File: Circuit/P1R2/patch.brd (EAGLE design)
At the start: 50.8 x 53.1 mm, 66 parts, among them U1 MK20DX256VLH7, U2 TPS61200, U3 MPU-9250, Y1 32.768KHz, Y2 16Mhz/8pF, Y3 16 Mhz, Y4 16 Mhz

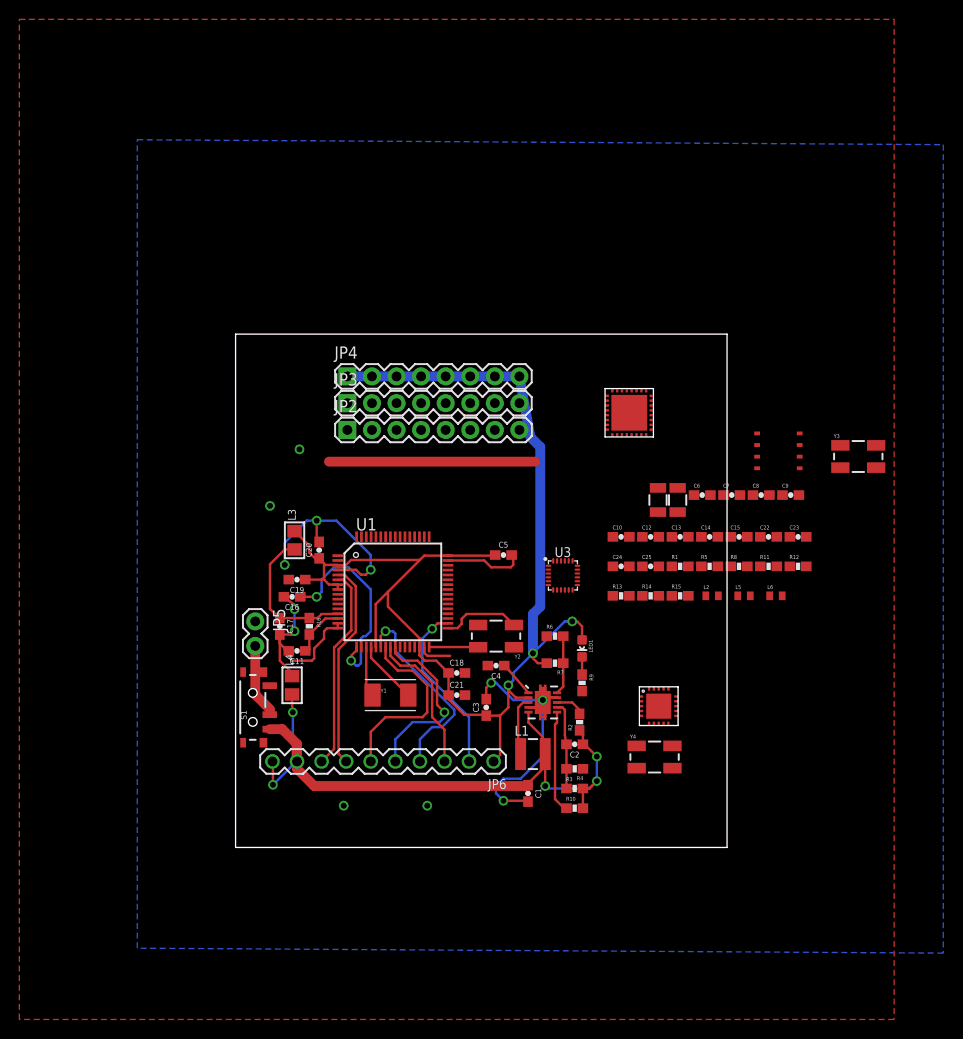
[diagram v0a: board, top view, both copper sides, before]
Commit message: Mesh and IMU in place
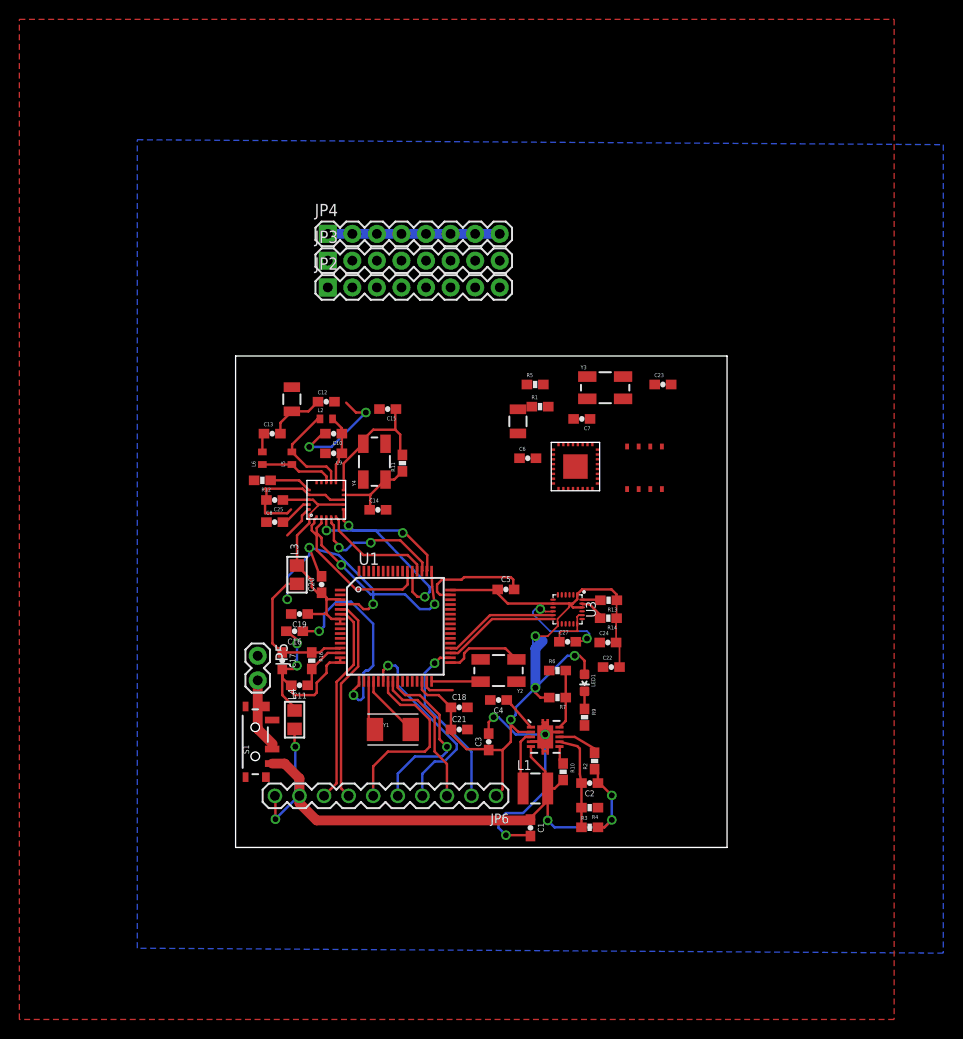
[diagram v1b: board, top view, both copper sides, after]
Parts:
- removed MESH: NRF24L01, RF:QFN20(4X4)
- removed R15: 10k, SparkFun-Resistors:0603-RES
- removed R8: 12k, SparkFun-Resistors:0603-RES
- removed WIFI: ESP8266EX, wifi:QFN32
- added C27: .1 uF, SparkFun-Capacitors:0603-CAP
- added U$4: NRF24L01, RF:QFN20(4X4)
- added U$6: ESP8266EX, wifi:QFN32
- Y3: value 16 Mhz -> 26 Mhz
- moved R12 56.1 mm to (2.77, 37.9), turned to 180 degrees
- moved L6 55.0 mm to (2.77, 40.2), turned to 90 degrees
- moved C8 50.4 mm to (4.04, 33.6)
- moved L5 48.9 mm to (5.82, 40.2), turned to 90 degrees
- moved C9 47.4 mm to (10.1, 40.7), turned to 180 degrees
- moved L2 43.9 mm to (9.37, 44.3)
- moved C13 43.5 mm to (3.78, 42.8)
- moved Y4 42.1 mm to (14.4, 39.9), turned to 90 degrees
- moved U$2 41.2 mm to (5.82, 46.3), turned to 180 degrees
- moved C25 39.5 mm to (4.04, 35.9), turned to 180 degrees
- moved R11 39.3 mm to (17.2, 39.7), turned to 90 degrees
- moved C15 38.6 mm to (15.7, 45.3), turned to 180 degrees
- moved C12 36.3 mm to (9.37, 46.1)
- moved C14 34.4 mm to (14.7, 34.9)
- moved C10 31.6 mm to (10.1, 42.8), turned to 180 degrees
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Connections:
- net 14 renamed PTD1
- net 2 renamed PTD0
- net 21 renamed PTD6
- net 23 renamed PTC2
- net 24 renamed PTA5
- net 26 renamed PTE1
- net 29 renamed PTC10
- net 3 renamed PTA12
- net 30 renamed PTC11
- net 31 renamed PTE0
- net 33 renamed PTA4
- net 4 renamed PTA13
- net 5 renamed PTD7
- net 6 renamed PTD4
- net 7 renamed PTD2
- net 8 renamed PTD3
- net 9 renamed PTC3
- net N$7 renamed PTD5
- removed net 0: U1.39
- removed net 1: U1.40
- removed net 10: U1.49
- removed net 11/MOSI: U1.51
- removed net 12/MISO: U1.52
- removed net 13/SCK: U1.50
- removed net 15: U1.43
- removed net 22: U1.44
- removed net 25: U1.42
- removed net 27: U1.54
- removed net 3.3V1: C22.2, C24.2, C25.1, MESH.15, MESH.18, MESH.7, R8.2, U$3.8, U3.1, U3.13, U3.8, WIFI.CHIP_EN/7, WIFI.VDD3P3/3, WIFI.VDD3P3/4, WIFI.VDDA/1, WIFI.VDDD/29, WIFI.VDDPST/11, WIFI.VDDPST/17
- removed net 32: U1.41
- removed net CE: MESH.1
- removed net CSN: MESH.2
- removed net GND1: C10.2, C12.2, C14.2, C15.2, C22.1, C23.2, C24.1, C25.2, C7.2, C8.1, C9.2, MESH.14, MESH.17, MESH.20, MESH.8, R12.2, R5.1, U$3.4, WIFI.GND
- removed net IQR: MESH.6
- removed net MISO: MESH.5
- removed net MOSI: MESH.4
- removed net N$22: MESH.GND
- removed net N$31: R8.1, WIFI.GPIO2/14
- removed net N$33: U3.11
- removed net N$35: U3.21
- removed net N$36: U3.7
- removed net N$37: U3.18, U3.20
- removed net N$39: U3.12
- removed net N$40: U3.22
- removed net RST: R1.1, WIFI.EXT_RSTB/32
- removed net RX_W: WIFI.U0TXD/26
- removed net SCK: MESH.3
- removed net SDO: R15.2
- removed net TX_W: WIFI.U0RXD/25
- new net PTB16: U$6.U0RXD/25, U1.39
- new net PTB17: U$6.U0TXD/26, U1.40
- new net PTB18: U$6.GPIO0/15, U1.41
- new net PTB19: U$6.GPIO2/14, U1.42
- new net PTC0: U$6.EXT_RSTB/32, U1.43
- new net PTC1: U$6.CHIP_EN/7, U1.44
- new net PTC4: U$4.2, U1.49
- new net PTC5: U$4.3, U1.50
- new net PTC6: U$4.4, U1.51
- new net PTC7: U$4.5, U1.52
- new net PTC8: U$4.6, U1.53
- new net PTC9: U$4.1, U1.54
- net 3.3V: now also C22.2, C24.2, C25.1, R13.1, R14.1, U$3.8, U$4.18, U$4.7, U$6.VDD3P3/3, U$6.VDD3P3/4, U$6.VDDA/1, U$6.VDDD/29, U$6.VDDPST/11, U$6.VDDPST/17, U3.1, U3.13, U3.22, U3.8
- net GND: now also C10.2, C12.2, C14.2, C15.2, C22.1, C23.2, C24.1, C25.2, C27.1, C7.2, C8.1, C9.2, R1.2, R12.2, R5.1, U$3.4, U$4.17, U$4.20, U$4.8, U$6.GND, U3.18, U3.20
- net N$13: now also U$6.LNA/2; no longer WIFI.LNA/2
- net N$17: now also U$4.9; no longer MESH.9
- net N$18: now also U$4.10; no longer MESH.10
- net N$19: now also U$4.11; no longer MESH.11
- net N$20: now also U$4.13; no longer MESH.13
- net N$21: now also U$4.19; no longer MESH.19
- net N$23: now also U$4.12; no longer MESH.12
- net N$24: now also U$4.16; no longer MESH.16
- net N$32: now also U$6.MTCK/12; no longer WIFI.MTCK/12
- net N$34: now also C27.2
- net N$38: now also R1.1, U$6.RES12K/31; no longer WIFI.RES12K/31
- net PTB0: now also U3.12
- net PTB1: now also U3.11
- net RTC: now also U$6.VDD_RTC/5; no longer WIFI.VDD_RTC/5
- net SCL: now also U3.23
- net SD-CLK: now also U$6.SD_CLK/21; no longer WIFI.SD_CLK/21
- net SD-CMD: now also U$6.SD_CMD/20; no longer WIFI.SD_CMD/20
- net SD-D0: now also U$6.SD_DATA_0/22; no longer WIFI.SD_DATA_0/22
- net SD-D1: now also U$6.SD_DATA_1/23; no longer WIFI.SD_DATA_1/23
- net SD-D2: now also U$6.SD_DATA_2/18; no longer WIFI.SD_DATA_2/18
- net SD-D3: now also U$6.SD_DATA_3/19; no longer WIFI.SD_DATA_3/19
- net SDA: now also U3.24
- net TOUT: now also U$6.TOUT/6; no longer WIFI.TOUT/6
- net VDD: now also U$6.VDDA/30; no longer R13.1, R14.1, R15.1, WIFI.VDDA/30
- net XTAL_IN: now also U$6.XTAL_IN/28; no longer WIFI.XTAL_IN/28
- net XTAL_OUT: now also U$6.XTAL_OUT/27; no longer WIFI.XTAL_OUT/27
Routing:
- net PTC4: track 0.00 -> 21.4 mm, vias 0 -> 2
- net GND: track 102.5 -> 121.1 mm, vias 8 -> 10
- net PTC8: track 0.00 -> 17.8 mm, vias 0 -> 2
- net PTC9: track 0.00 -> 16.5 mm
- net N$18: track 0.00 -> 14.9 mm
- net PTC5: track 0.00 -> 14.5 mm, vias 0 -> 2
- net PTC6: track 0.00 -> 14.5 mm, vias 0 -> 2
- net PTB0: track 0.00 -> 12.1 mm
- net PTB1: track 0.00 -> 12.0 mm
- net PTC7: track 0.00 -> 11.7 mm
- net N$34: track 0.00 -> 11.1 mm, vias 0 -> 2
- net N$23: track 0.00 -> 10.8 mm
- net 3.3V: track 132.9 -> 122.9 mm, vias 4 -> 5
- net SOFTPOWER: track 10.7 -> 1.93 mm
- net N$17: track 0.00 -> 8.65 mm
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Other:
- board size 50.8 x 53.1 mm -> 50.8 x 50.8 mm

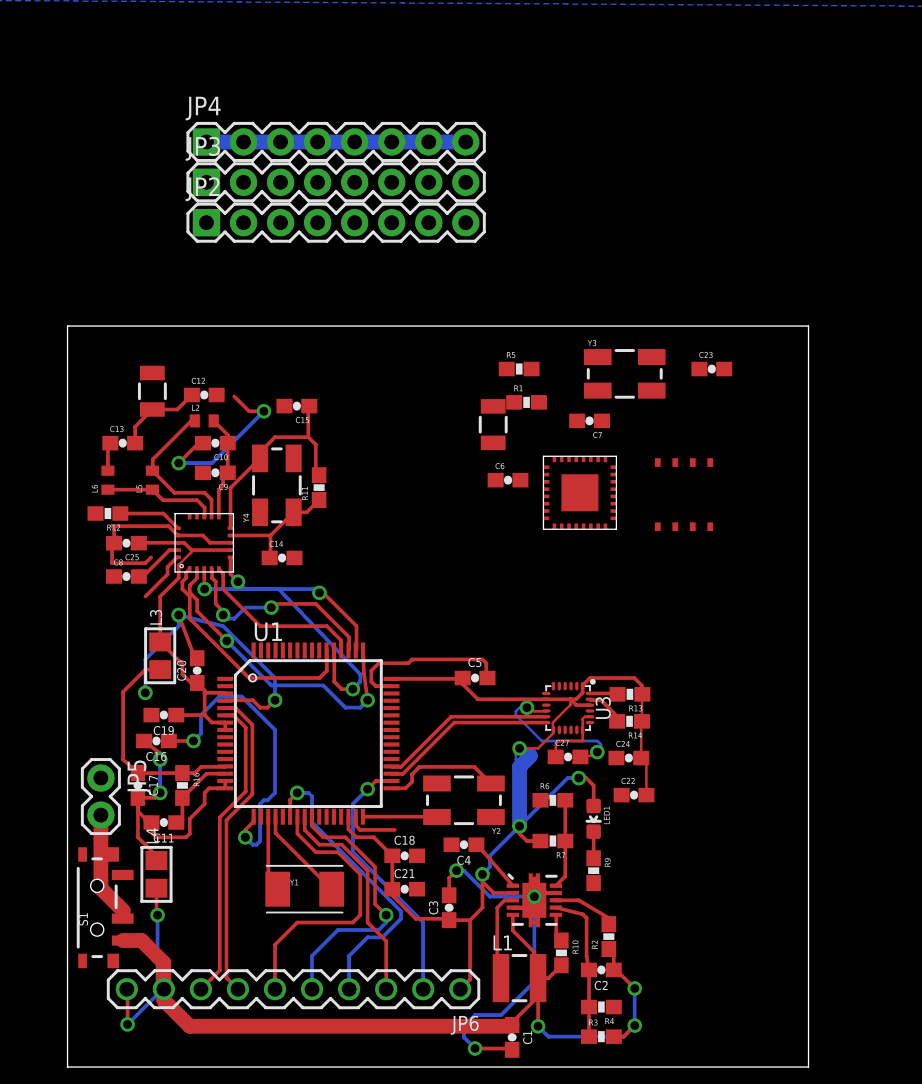
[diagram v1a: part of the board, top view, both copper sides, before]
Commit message: Communications and IMU done. Finishing up GPIO next
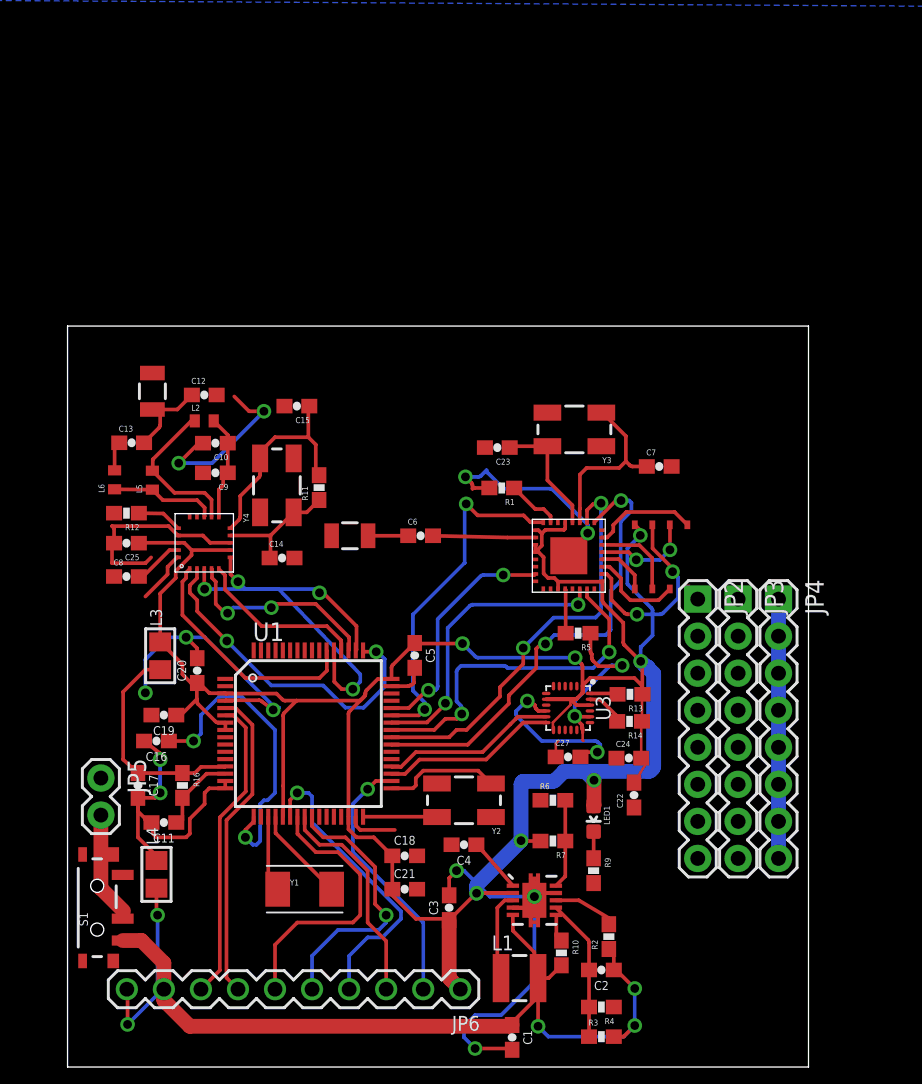
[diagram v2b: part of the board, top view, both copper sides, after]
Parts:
- moved JP4 50.2 mm to (48.7, 32.1), turned to 270 degrees
- moved JP3 46.3 mm to (46.0, 32.1), turned to 270 degrees
- moved JP2 42.4 mm to (43.2, 32.1), turned to 270 degrees
- moved R5 18.6 mm to (35.0, 29.7), turned to 180 degrees
- moved C23 15.7 mm to (29.5, 42.5), turned to 180 degrees
- moved U$1 12.4 mm to (19.4, 36.4), turned to 270 degrees
- moved C6 7.10 mm to (24.2, 36.4)
- moved R1 6.11 mm to (29.8, 39.7), turned to 180 degrees
- moved C7 5.71 mm to (40.6, 41.2), turned to 0 degrees
- moved Y3 5.14 mm to (34.7, 43.7), turned to 180 degrees
- moved U$3 4.55 mm to (40.7, 35.0)
- moved C5 4.42 mm to (23.8, 28.2), turned to 270 degrees
- moved U$6 4.38 mm to (34.4, 35.1)
- moved R12 1.27 mm to (4.04, 38.0)
- moved C13 0.61 mm to (4.39, 42.8)
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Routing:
- net 3.3V: track 122.9 -> 197.3 mm, vias 5 -> 8
- net PTB16: track 0.00 -> 31.9 mm, vias 0 -> 2
- net PTB17: track 0.00 -> 28.4 mm, vias 0 -> 2
- net PTB18: track 0.00 -> 24.4 mm, vias 0 -> 2
- net PTC0: track 0.00 -> 24.2 mm, vias 0 -> 2
- net PTB19: track 0.00 -> 20.2 mm, vias 0 -> 2
- net PTC1: track 0.00 -> 16.4 mm, vias 0 -> 2
- net SD-D2: track 0.00 -> 13.4 mm, vias 0 -> 2
- net XTAL_OUT: track 0.00 -> 12.4 mm
- net GND: track 121.1 -> 133.2 mm, vias 10 -> 14
- net XTAL_IN: track 0.00 -> 8.53 mm
- net SD-D1: track 0.00 -> 7.16 mm
- net N$13: track 0.00 -> 7.01 mm
- net SD-CLK: track 0.00 -> 6.86 mm, vias 0 -> 2
- net SD-D3: track 0.00 -> 6.40 mm
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
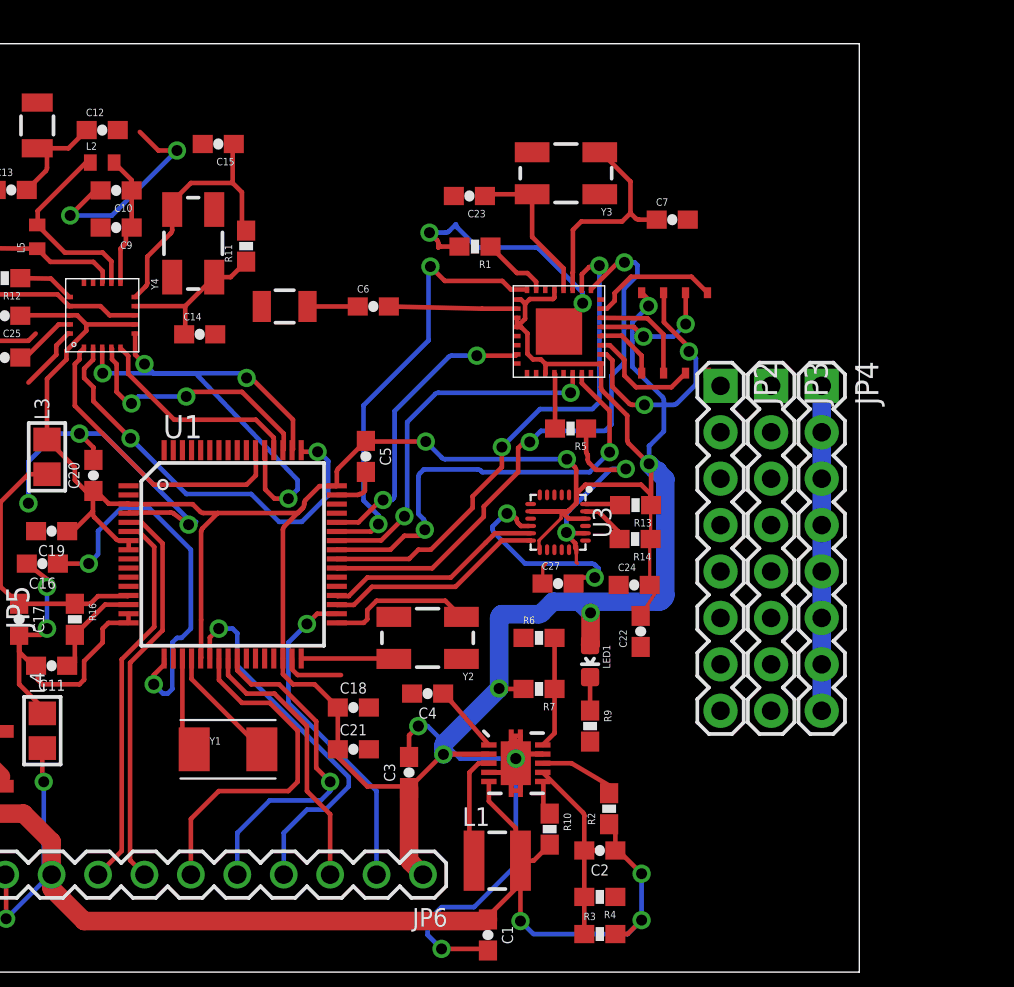
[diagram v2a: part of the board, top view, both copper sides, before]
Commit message: Made space for GPIO. Putting in GPIO and RGB leds
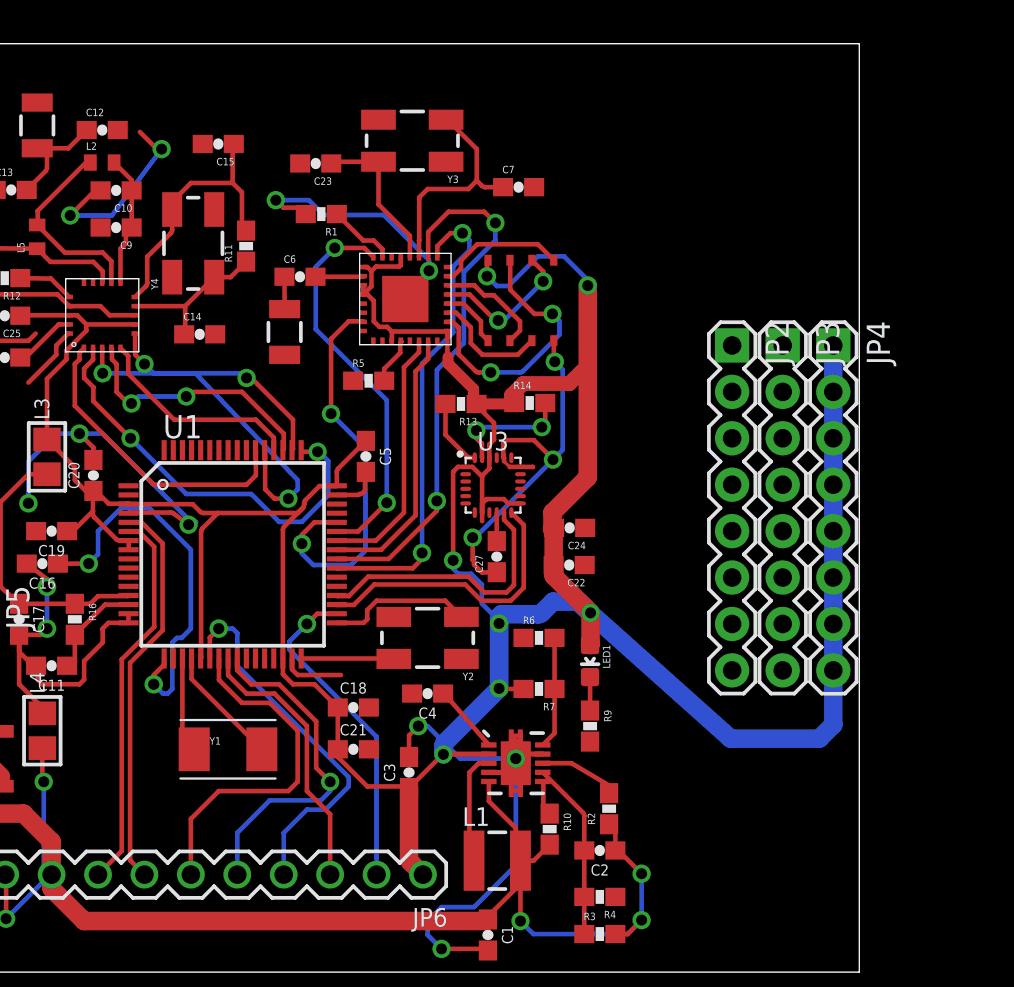
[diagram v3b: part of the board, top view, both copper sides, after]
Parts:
- moved R5 11.4 mm to (24.0, 32.4), turned to 0 degrees
- moved R13 11.0 mm to (29.0, 31.1)
- moved R14 9.41 mm to (32.8, 31.1), turned to 0 degrees
- moved C7 8.59 mm to (32.2, 43.0)
- moved U$3 8.59 mm to (32.3, 36.8)
- moved C23 8.59 mm to (21.1, 44.2)
- moved R1 8.59 mm to (21.4, 41.5)
- moved U$6 8.59 mm to (26.0, 36.8)
- moved Y3 8.59 mm to (26.3, 45.5)
- moved C22 5.34 mm to (34.9, 22.3), turned to 180 degrees
- moved C24 4.71 mm to (35.0, 24.3), turned to 180 degrees
- moved C6 4.33 mm to (20.2, 38.0)
- moved U3 4.10 mm to (30.8, 26.6), turned to 0 degrees
- moved C27 3.66 mm to (31.0, 22.7), turned to 90 degrees
- moved JP2 2.30 mm to (43.8, 34.3)
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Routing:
- net N$34: track 11.4 -> 1.56 mm, vias 2 -> 0
- net PTB18: track 24.4 -> 14.9 mm, vias 2 -> 0
- net 3.3V: track 197.3 -> 206.2 mm
- net GND: track 133.2 -> 139.8 mm, vias 14 -> 15
- net PTB19: track 20.2 -> 14.0 mm, vias 2 -> 0
- net PTB16: track 31.9 -> 26.2 mm
- net PTC1: track 16.4 -> 21.8 mm
- net N$3: track 0.00 -> 5.17 mm
- net N$13: track 7.01 -> 2.63 mm
- net SCL: track 2.67 -> 6.72 mm, vias 0 -> 2
- net PTB0: track 12.1 -> 15.8 mm
- net PTB1: track 12.0 -> 14.9 mm
- net PTC0: track 24.2 -> 21.7 mm
- net SDA: track 1.90 -> 3.81 mm
- net SD-D2: track 13.4 -> 14.7 mm
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
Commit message: GPIO wired yo
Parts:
- moved JP5 10.4 mm to (2.29, 30.2)
- moved C15 5.26 mm to (11.0, 47.7)
- moved R11 4.67 mm to (15.6, 44.1)
- moved C14 3.93 mm to (12.4, 38.1)
- moved U$2 3.80 mm to (2.26, 47.7)
- moved Y4 3.76 mm to (12.3, 43.0)
- moved C12 3.68 mm to (6.07, 47.7)
- moved C10 2.76 mm to (7.70, 44.1)
- moved C9 2.75 mm to (7.70, 42.0)
- moved C13 2.23 mm to (2.74, 44.3)
- moved C25 2.23 mm to (2.39, 37.4)
- moved R12 2.23 mm to (2.39, 39.5)
- moved L2 2.23 mm to (7.72, 45.8)
- moved U$4 2.23 mm to (7.72, 37.4)
- moved L6 2.23 mm to (1.57, 41.8)
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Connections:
- net PTC10: now also JP2.8
- net PTC11: now also JP2.7
- net PTD0: now also JP2.6
- net PTD1: now also JP2.5
- net PTD2: now also JP2.4
- net PTD3: now also JP2.3
- net PTD4: now also JP2.2
- net PTD5: now also JP2.1
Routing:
- net PTD0: track 0.00 -> 73.7 mm, vias 0 -> 1
- net PTC11: track 0.00 -> 73.1 mm, vias 0 -> 1
- net PTC10: track 0.00 -> 72.8 mm, vias 0 -> 1
- net PTD3: track 0.00 -> 69.5 mm, vias 0 -> 1
- net PTD2: track 0.00 -> 69.4 mm, vias 0 -> 1
- net PTD1: track 0.00 -> 69.2 mm, vias 0 -> 3
- net PTD4: track 0.00 -> 68.8 mm, vias 0 -> 1
- net PTD5: track 0.00 -> 67.0 mm, vias 0 -> 1
- net 3.3V: track 206.2 -> 245.2 mm, vias 8 -> 10
- net N$4: track 0.00 -> 18.6 mm
- net VRAW: track 7.76 -> 18.2 mm
- net GND: track 139.8 -> 149.4 mm, vias 15 -> 14
- net PTC5: track 14.5 -> 19.1 mm
- net PTC8: track 17.8 -> 22.4 mm
- net PTC7: track 11.7 -> 15.0 mm, vias 0 -> 2
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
